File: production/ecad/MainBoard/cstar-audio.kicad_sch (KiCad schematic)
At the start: 4 parts, among them J1 532610771, J2 Conn_01x03_Pin, J3 Conn_01x03_Pin, J4 532610771

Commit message: footprint assignments
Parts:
- J1, J4: footprint 532610771:MOLEX_532610771 -> CSTAR-MainBoard-Footprints:MOLEX_532610771
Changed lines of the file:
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@@
       (effects (font (size 1.27 1.27)) (justify left))
     )
-    (property "Footprint" "532610771:MOLEX_532610771" (at 217.17 99.06 0)
+    (property "Footprint" "CSTAR-MainBoard-Footprints:MOLEX_532610771" (at 217.17 99.06 0)
       (effects (font (size 1.27 1.27)) (justify bottom) hide)
     )
@@
       (project "CSTAR"
         (path "/cd9fa943-c6eb-468b-990c-ea873c442553/2cc69299-a9af-44e6-bcb8-323a1f2cc303"
-          (reference "#PWR0126") (unit 1)
+          (reference "#PWR0118") (unit 1)
         )
       )
@@
       (project "CSTAR"
         (path "/cd9fa943-c6eb-468b-990c-ea873c442553/2cc69299-a9af-44e6-bcb8-323a1f2cc303"
-          (reference "#PWR0127") (unit 1)
+          (reference "#PWR0119") (unit 1)
         )
       )
@@
       (project "CSTAR"
         (path "/cd9fa943-c6eb-468b-990c-ea873c442553/2cc69299-a9af-44e6-bcb8-323a1f2cc303"
-          (reference "#PWR0125") (unit 1)
+          (reference "#PWR0117") (unit 1)
         )
       )
@@
       (project "CSTAR"
         (path "/cd9fa943-c6eb-468b-990c-ea873c442553/2cc69299-a9af-44e6-bcb8-323a1f2cc303"
-          (reference "#PWR0128") (unit 1)
+          (reference "#PWR0120") (unit 1)
         )
       )
@@
       (project "CSTAR"
         (path "/cd9fa943-c6eb-468b-990c-ea873c442553/2cc69299-a9af-44e6-bcb8-323a1f2cc303"
-          (reference "#PWR0130") (unit 1)
+          (reference "#PWR0122") (unit 1)
         )
       )
@@
       (project "CSTAR"
         (path "/cd9fa943-c6eb-468b-990c-ea873c442553/2cc69299-a9af-44e6-bcb8-323a1f2cc303"
-          (reference "#PWR0129") (unit 1)
+          (reference "#PWR0121") (unit 1)
         )
       )
@@
       (effects (font (size 1.27 1.27)) (justify left))
     )
-    (property "Footprint" "532610771:MOLEX_532610771" (at 80.01 101.6 0)
-      (effects (font (size 1.27 1.27)) (justify bottom) hide)
-    )
+    (property "Footprint" "CSTAR-MainBoard-Footprints:MOLEX_532610771" (at 80.01 101.6 0)
+      (effects (font (size 1.27 1.27)) (justify bottom) hide)
+    )

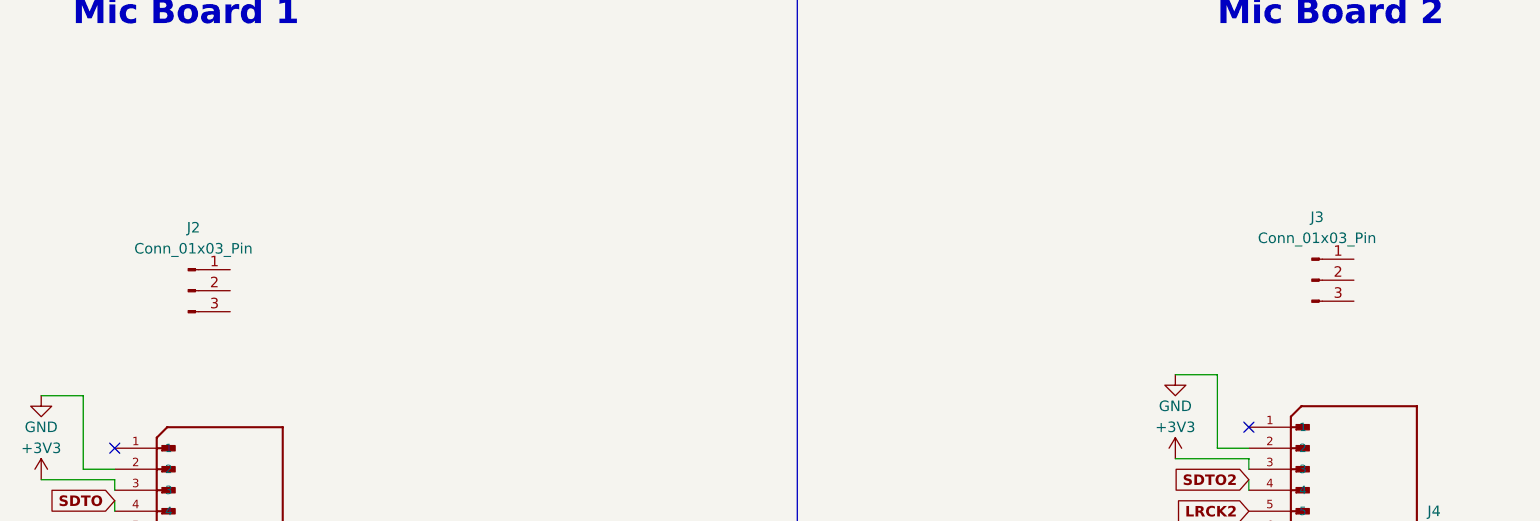
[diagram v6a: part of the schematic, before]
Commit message: footprint assign more
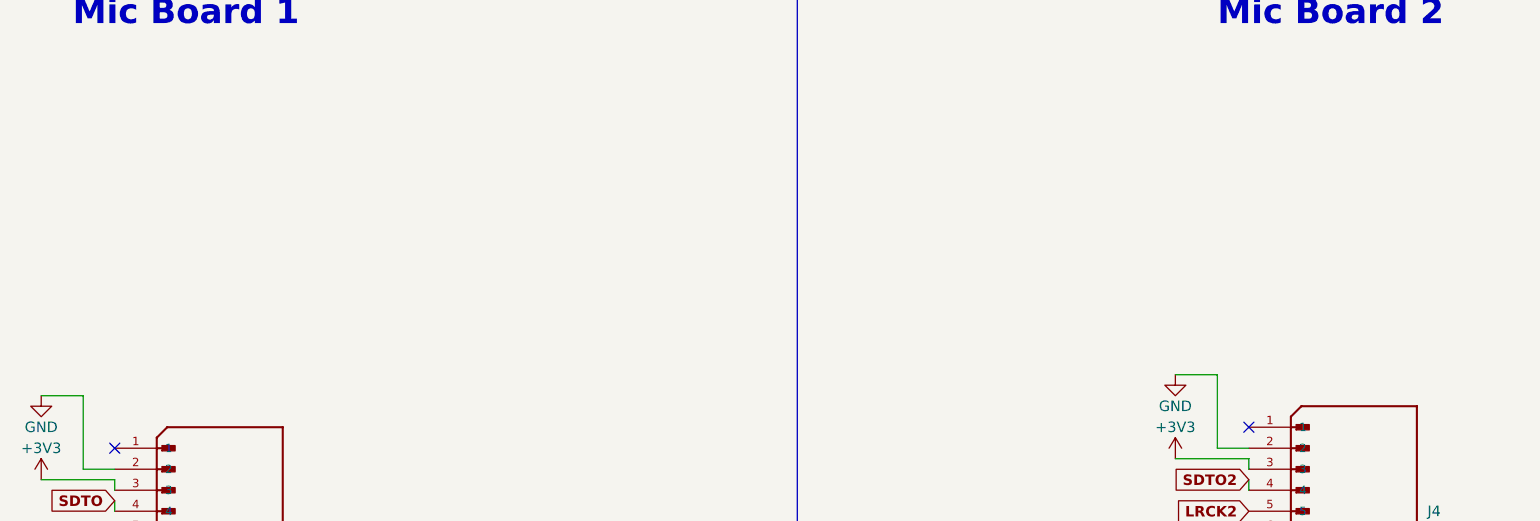
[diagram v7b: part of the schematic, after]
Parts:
- removed J2, J3: Conn_01x03_Pin, Connector_Phoenix_SPT:PhoenixContact_SPT_1.5_9-H-3.5_1x09_P3.5mm_Horizontal, symbol Connector:Conn_01x03_Pin
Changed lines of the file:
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@@
-    )
-  )
-  (symbol (lib_id "Connector:Conn_01x03_Pin") (at 212.09 71.12 0) (unit 1)
-    (in_bom yes) (on_board yes) (dnp no) (fields_autoplaced)
-    (property "Reference" "J3" (at 212.725 63.5 0)
-      (effects (font (size 1.27 1.27)))
-    )
-    (property "Value" "Conn_01x03_Pin" (at 212.725 66.04 0)
-      (effects (font (size 1.27 1.27)))
-    )
-    (property "Footprint" "Connector_Phoenix_SPT:PhoenixContact_SPT_1.5_9-H-3.5_1x09_P3.5mm_Horizontal" (at 212.09 71.12 0)
-      (effects (font (size 1.27 1.27)) hide)
-    )
-    (property "Datasheet" "~" (at 212.09 71.12 0)
-      (effects (font (size 1.27 1.27)) hide)
-    )
-    (pin "1")
-    (pin "2")
-    (pin "3")
-    (instances
-      (project "cstar-audio"
-        (path "/16a488a1-12e9-4eb7-bbd0-d500eeb9c89a"
-          (reference "J3") (unit 1)
-        )
-      )
-      (project "CSTAR"
-        (path "/cd9fa943-c6eb-468b-990c-ea873c442553/2cc69299-a9af-44e6-bcb8-323a1f2cc303"
-          (reference "J27") (unit 1)
-        )
-      )
-    )
-  )
-  (symbol (lib_id "Connector:Conn_01x03_Pin") (at 76.2 72.39 0) (unit 1)
-    (in_bom yes) (on_board yes) (dnp no) (fields_autoplaced)
-    (property "Reference" "J2" (at 76.835 64.77 0)
-      (effects (font (size 1.27 1.27)))
-    )
-    (property "Value" "Conn_01x03_Pin" (at 76.835 67.31 0)
-      (effects (font (size 1.27 1.27)))
-    )
-    (property "Footprint" "Connector_Phoenix_SPT:PhoenixContact_SPT_1.5_9-H-3.5_1x09_P3.5mm_Horizontal" (at 76.2 72.39 0)
-      (effects (font (size 1.27 1.27)) hide)
-    )
-    (property "Datasheet" "~" (at 76.2 72.39 0)
-      (effects (font (size 1.27 1.27)) hide)
-    )
-    (pin "1")
-    (pin "2")
-    (pin "3")
-    (instances
-      (project "cstar-audio"
-        (path "/16a488a1-12e9-4eb7-bbd0-d500eeb9c89a"
-          (reference "J2") (unit 1)
-        )
-      )
-      (project "CSTAR"
-        (path "/cd9fa943-c6eb-468b-990c-ea873c442553/2cc69299-a9af-44e6-bcb8-323a1f2cc303"
-          (reference "J25") (unit 1)
-        )
-      )
     )
   )

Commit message: initial mic layout
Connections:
- net LRCK2 is gone; now on net I2S_CLK: J4.5
- net MCLK2 is gone; now on net I2S_CMD: J4.6
- net BICK renamed I2S_D0
- net BICK2 renamed I2S_D1
- net LRCK renamed I2S_CLK
- net MCLK renamed I2S_CMD
- net SDTO renamed I2S_D2
- net SDTO2 renamed I2S_D3
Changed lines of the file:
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@@
     (effects (font (size 3 3) (thickness 0.6) bold) (justify left bottom))
   )
-  (global_label "MCLK2" (shape input) (at 204.47 102.87 180) (fields_autoplaced)
+  (global_label "I2S_CMD" (shape input) (at 204.47 102.87 180) (fields_autoplaced)
     (effects (font (size 1.27 1.27) bold) (justify right))
-    (property "Intersheetrefs" "${INTERSHEET_REFS}" (at 194.7798 102.87 0)
+    (property "Intersheetrefs" "${INTERSHEET_REFS}" (at 193.026 102.87 0)
       (effects (font (size 1.27 1.27)) (justify right) hide)
     )
   )
-  (global_label "LRCK" (shape input) (at 67.31 101.6 180) (fields_autoplaced)
+  (global_label "I2S_CLK" (shape input) (at 67.31 101.6 180) (fields_autoplaced)
     (effects (font (size 1.27 1.27) bold) (justify right))
-    (property "Intersheetrefs" "${INTERSHEET_REFS}" (at 59.0107 101.6 0)
+    (property "Intersheetrefs" "${INTERSHEET_REFS}" (at 56.2893 101.6 0)
       (effects (font (size 1.27 1.27)) (justify right) hide)
     )
   )
-  (global_label "SDTO" (shape input) (at 67.31 97.79 180) (fields_autoplaced)
+  (global_label "I2S_D2" (shape input) (at 67.31 97.79 180) (fields_autoplaced)
     (effects (font (size 1.27 1.27) bold) (justify right))
-    (property "Intersheetrefs" "${INTERSHEET_REFS}" (at 59.0712 97.79 0)
+    (property "Intersheetrefs" "${INTERSHEET_REFS}" (at 57.3779 97.79 0)
       (effects (font (size 1.27 1.27)) (justify right) hide)
     )
   )
-  (global_label "LRCK2" (shape input) (at 204.47 99.06 180) (fields_autoplaced)
+  (global_label "I2S_CLK" (shape input) (at 204.47 99.06 180) (fields_autoplaced)
     (effects (font (size 1.27 1.27) bold) (justify right))
-    (property "Intersheetrefs" "${INTERSHEET_REFS}" (at 194.9612 99.06 0)
+    (property "Intersheetrefs" "${INTERSHEET_REFS}" (at 193.4493 99.06 0)
       (effects (font (size 1.27 1.27)) (justify right) hide)
     )
   )
-  (global_label "MCLK" (shape input) (at 67.31 105.41 180) (fields_autoplaced)
+  (global_label "I2S_CMD" (shape input) (at 67.31 105.41 180) (fields_autoplaced)
     (effects (font (size 1.27 1.27) bold) (justify right))
-    (property "Intersheetrefs" "${INTERSHEET_REFS}" (at 58.8293 105.41 0)
+    (property "Intersheetrefs" "${INTERSHEET_REFS}" (at 55.866 105.41 0)
       (effects (font (size 1.27 1.27)) (justify right) hide)
     )
   )
-  (global_label "BICK" (shape input) (at 67.31 109.22 180) (fields_autoplaced)
+  (global_label "I2S_D0" (shape input) (at 67.31 109.22 180) (fields_autoplaced)
     (effects (font (size 1.27 1.27) bold) (justify right))
-    (property "Intersheetrefs" "${INTERSHEET_REFS}" (at 59.434 109.22 0)
+    (property "Intersheetrefs" "${INTERSHEET_REFS}" (at 57.3779 109.22 0)
       (effects (font (size 1.27 1.27)) (justify right) hide)
     )
   )
-  (global_label "BICK2" (shape input) (at 204.47 106.68 180) (fields_autoplaced)
+  (global_label "I2S_D1" (shape input) (at 204.47 106.68 180) (fields_autoplaced)
     (effects (font (size 1.27 1.27) bold) (justify right))
-    (property "Intersheetrefs" "${INTERSHEET_REFS}" (at 195.3845 106.68 0)
+    (property "Intersheetrefs" "${INTERSHEET_REFS}" (at 194.5379 106.68 0)
       (effects (font (size 1.27 1.27)) (justify right) hide)
     )
   )
-  (global_label "SDTO2" (shape input) (at 204.47 95.25 180) (fields_autoplaced)
+  (global_label "I2S_D3" (shape input) (at 204.47 95.25 180) (fields_autoplaced)
     (effects (font (size 1.27 1.27) bold) (justify right))
-    (property "Intersheetrefs" "${INTERSHEET_REFS}" (at 195.0217 95.25 0)
+    (property "Intersheetrefs" "${INTERSHEET_REFS}" (at 194.5379 95.25 0)
       (effects (font (size 1.27 1.27)) (justify right) hide)
     )
